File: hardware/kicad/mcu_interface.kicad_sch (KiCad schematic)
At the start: 1 part, among them U1 ESP32-S3-DevKitC-1

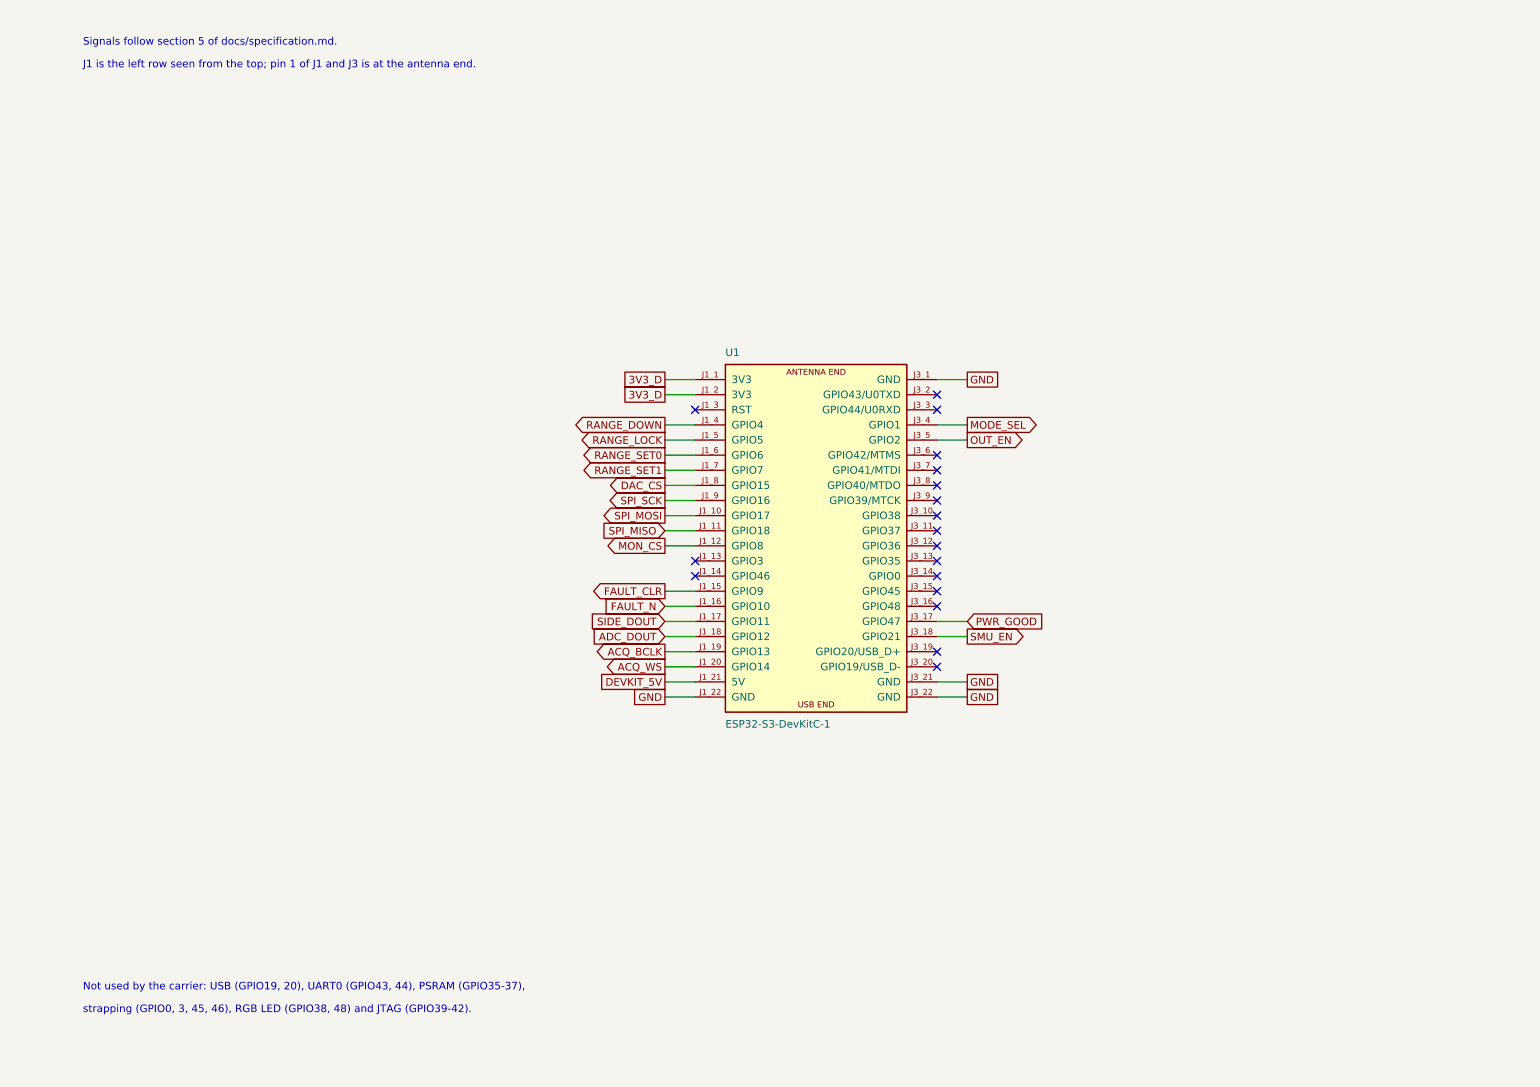
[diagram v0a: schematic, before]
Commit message: feat(hardware): draw the carrier board schematic as draft A0
Draw every block of the carrier board on thirteen A4 sheets: board
interface, power input, analog rails, source meter, path switching,
shunt ladder, output stage, signal chain, comparators, range logic,
digital inputs and monitors. Connections inside a sheet are wires,
supply rails use power symbols, and the root sheet joins the sheets
with wires between their hierarchical pins.

This is a review draft, drawn at the request of the project owner
before the component checks are closed. The parts are the candidates
of the specification, nothing was simulated or measured, and the logic
device that holds the range logic has no description yet.

The electrical rules check reports no errors and no warnings.
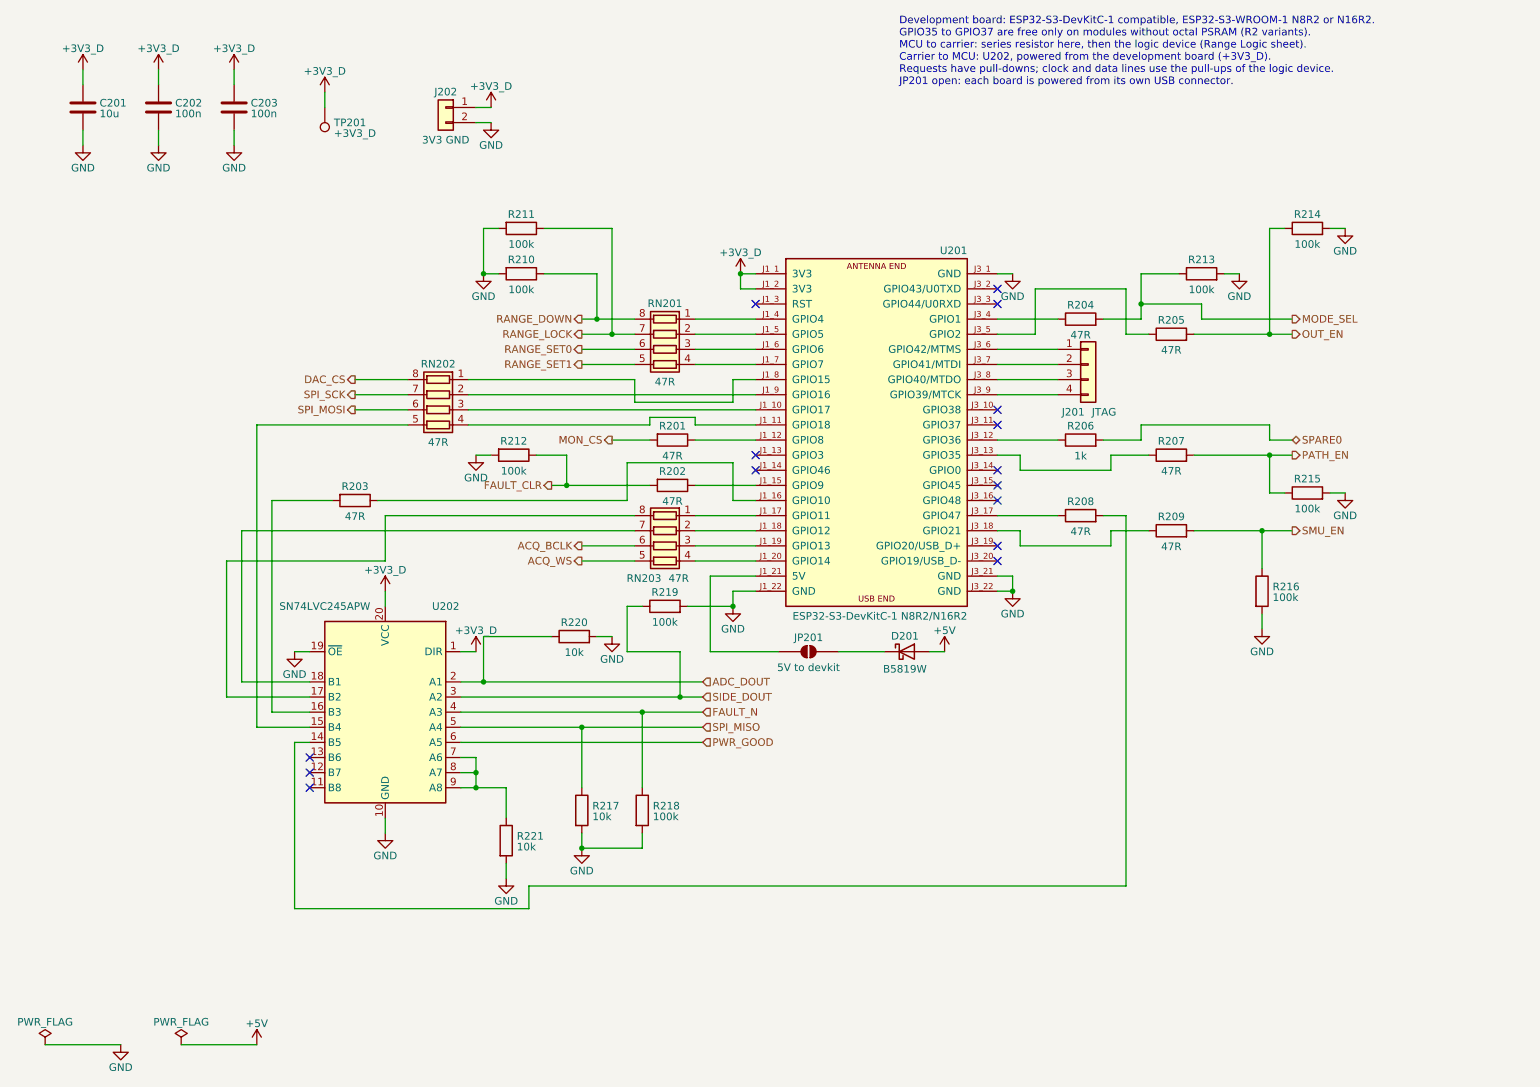
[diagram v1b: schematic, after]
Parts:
- removed U1: ESP32-S3-DevKitC-1, PowerProfiler:ESP32-S3-DevKitC-1_Socket, symbol PowerProfiler:ESP32-S3-DevKitC-1
- added C201: 10u, Capacitor_SMD:C_0805_2012Metric, symbol Device:C
- added C202, C203: 100n, Capacitor_SMD:C_0603_1608Metric, symbol Device:C
- added D201: B5819W, Diode_SMD:D_SOD-123, symbol Device:D_Schottky
- added J201: JTAG, Connector_PinHeader_2.54mm:PinHeader_1x04_P2.54mm_Vertical, symbol Connector_Generic:Conn_01x04
- added J202: 3V3 GND, Connector_PinHeader_2.54mm:PinHeader_1x02_P2.54mm_Vertical, symbol Connector_Generic:Conn_01x02
- added JP201: 5V to devkit, Jumper:SolderJumper-2_P1.3mm_Open_RoundedPad1.0x1.5mm, symbol Jumper:SolderJumper_2_Open
- added R201, R202, R203, R204, R205, R207, R208, R209: 47R, Resistor_SMD:R_0603_1608Metric, symbol Device:R
- added R206: 1k, Resistor_SMD:R_0603_1608Metric, symbol Device:R
- added R210, R211, R212, R213, R214, R215, R216, R218, R219: 100k, Resistor_SMD:R_0603_1608Metric, symbol Device:R
- added R217, R220, R221: 10k, Resistor_SMD:R_0603_1608Metric, symbol Device:R
- added RN201, RN202, RN203: 47R, Resistor_SMD:R_Array_Convex_4x0603, symbol Device:R_Pack04
- added TP201: +3V3_D, TestPoint:TestPoint_Pad_D1.5mm, symbol Connector:TestPoint
- added U201: ESP32-S3-DevKitC-1 N8R2/N16R2, PowerProfiler:ESP32-S3-DevKitC-1_Socket, symbol PowerProfiler:ESP32-S3-DevKitC-1
- added U202: SN74LVC245APW, Package_SO:TSSOP-20_4.4x6.5mm_P0.65mm, symbol Logic_LevelTranslator:SN74LVC245APW
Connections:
- net ACQ_BCLK: now also RN203.6 (R3.2)
- net ACQ_WS: now also RN203.5 (R4.2)
- net ADC_DOUT: now also R220.1, U202.2 (A1)
- net DAC_CS: now also RN202.8 (R1.2)
- net FAULT_CLR: now also R202.2, R212.1
- net FAULT_N: now also R218.1, U202.4 (A3)
- net GND: now also C201.2, C202.2, C203.2, J202.2 (Pin_2), R210.2, R211.2, R212.2, R213.2, R214.2, R215.2, R216.2, R217.2, R218.2, R219.2, R220.2, R221.2, U201.J1_22 (GND), U201.J3_1 (GND), U201.J3_21 (GND), U201.J3_22 (GND), U202.10 (GND), U202.19 (~{OE})
- net MODE_SEL: now also R204.2, R213.1
- net MON_CS: now also R201.2
- net OUT_EN: now also R205.2, R214.1
- net PWR_GOOD: now also U202.6 (A5)
- net RANGE_DOWN: now also R210.1, RN201.8 (R1.2)
- net RANGE_LOCK: now also R211.1, RN201.7 (R2.2)
- net RANGE_SET0: now also RN201.6 (R3.2)
- net RANGE_SET1: now also RN201.5 (R4.2)
- net SIDE_DOUT: now also R219.1, U202.3 (A2)
- net SMU_EN: now also R209.2, R216.1
- net SPI_MISO: now also R217.1, U202.5 (A4)
- net SPI_MOSI: now also RN202.6 (R3.2)
- net SPI_SCK: now also RN202.7 (R2.2)
- new net: D201.1 (K), JP201.1 (A)
- new net: JP201.2 (B), U201.J1_21 (5V)
- new net: RN201.1 (R1.1), U201.J1_4 (GPIO4)
- new net: RN201.2 (R2.1), U201.J1_5 (GPIO5)
- new net: RN201.3 (R3.1), U201.J1_6 (GPIO6)
- new net: RN201.4 (R4.1), U201.J1_7 (GPIO7)
- new net: R206.1, U201.J3_12 (GPIO36)
- new net: R207.1, U201.J3_13 (GPIO35)
- new net: J201.1 (Pin_1), U201.J3_6 (GPIO42/MTMS)
- new net: J201.2 (Pin_2), U201.J3_7 (GPIO41/MTDI)
- new net: J201.3 (Pin_3), U201.J3_8 (GPIO40/MTDO)
- new net: J201.4 (Pin_4), U201.J3_9 (GPIO39/MTCK)
- new net: R203.1, U201.J1_16 (GPIO10)
- new net: R203.2, U202.16 (B3)
- new net: R208.1, U201.J3_17 (GPIO47)
- new net: R208.2, U202.14 (B5)
- new net: RN202.3 (R3.1), U201.J1_10 (GPIO17)
- new net: RN202.4 (R4.1), U201.J1_11 (GPIO18)
- new net: R201.1, U201.J1_12 (GPIO8)
- new net: R202.1, U201.J1_15 (GPIO9)
- new net: RN203.1 (R1.1), U201.J1_17 (GPIO11)
- new net: RN203.2 (R2.1), U201.J1_18 (GPIO12)
- new net: RN203.3 (R3.1), U201.J1_19 (GPIO13)
- new net: RN203.4 (R4.1), U201.J1_20 (GPIO14)
- new net: RN202.1 (R1.1), U201.J1_8 (GPIO15)
- new net: RN202.2 (R2.1), U201.J1_9 (GPIO16)
- new net: R209.1, U201.J3_18 (GPIO21)
- new net: R204.1, U201.J3_4 (GPIO1)
- new net: R205.1, U201.J3_5 (GPIO2)
- new net: RN203.7 (R2.2), U202.18 (B1)
- new net: RN203.8 (R1.2), U202.17 (B2)
- new net: R221.1, U202.7 (A6), U202.8 (A7), U202.9 (A8)
- new net: RN202.5 (R4.2), U202.15 (B4)
- new net +3V3_D: C201.1, C202.1, C203.1, J202.1 (Pin_1), TP201.1, U201.J1_1 (3V3), U201.J1_2 (3V3), U202.1 (DIR), U202.20 (VCC)
- new net +5V: D201.2 (A)
- new net PATH_EN: R207.2, R215.1
- new net SPARE0: R206.2
- no-connect marks 18 -> 15
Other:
- note added: "Development board: ESP32-S3-DevKitC-1 compatible, ESP32-S3-WROOM-1 N8R2 or N16R2. GPIO35 to GPIO37 are free only on modules without octal PSRAM (R2 variants). MCU to carrier: series resistor here, then the logic device (Range Logic sheet). Carrier to MCU: U202, powered from the development board (+3V3_D). Requests have pull-downs; clock and data lines use the pull-ups of the logic device. JP201 o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"
- note removed: "J1 is the left row seen from the top; pin 1 of J1 and J3 is at the antenna end."
- note removed: "Not used by the carrier: USB (GPIO19, 20), UART0 (GPIO43, 44), PSRAM (GPIO35-37),"
- note removed: "Signals follow section 5 of docs/specification.md."
- note removed: "strapping (GPIO0, 3, 45, 46), RGB LED (GPIO38, 48) and JTAG (GPIO39-42)."
- title: Power Profiler Carrier - MCU Interface -> Development Board Interface
